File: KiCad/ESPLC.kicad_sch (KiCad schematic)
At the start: 51 parts, among them J1 D1, J10 A2, J11 USB_C_Receptacle_USB2.0_16P, J2 D2, J3 D3, J4 D4, J5 Screw_Terminal_01x03, J6 Screw_Terminal_01x03, J7 Screw_Terminal_01x03, J8 Screw_Terminal_01x03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

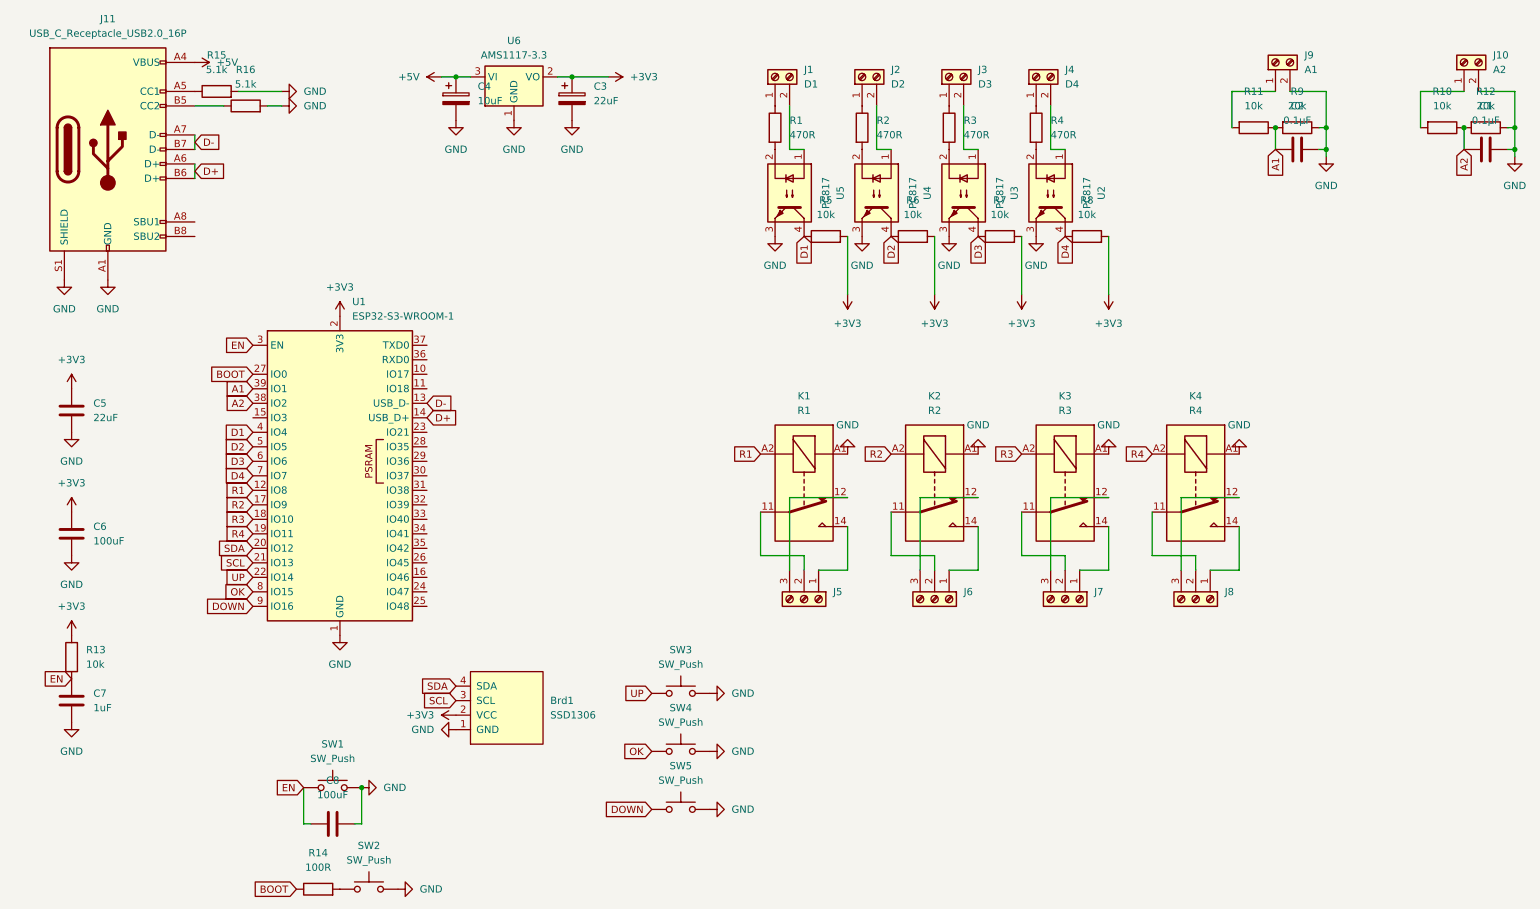
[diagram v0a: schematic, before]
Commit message: Added Software section to README, updated Gerber
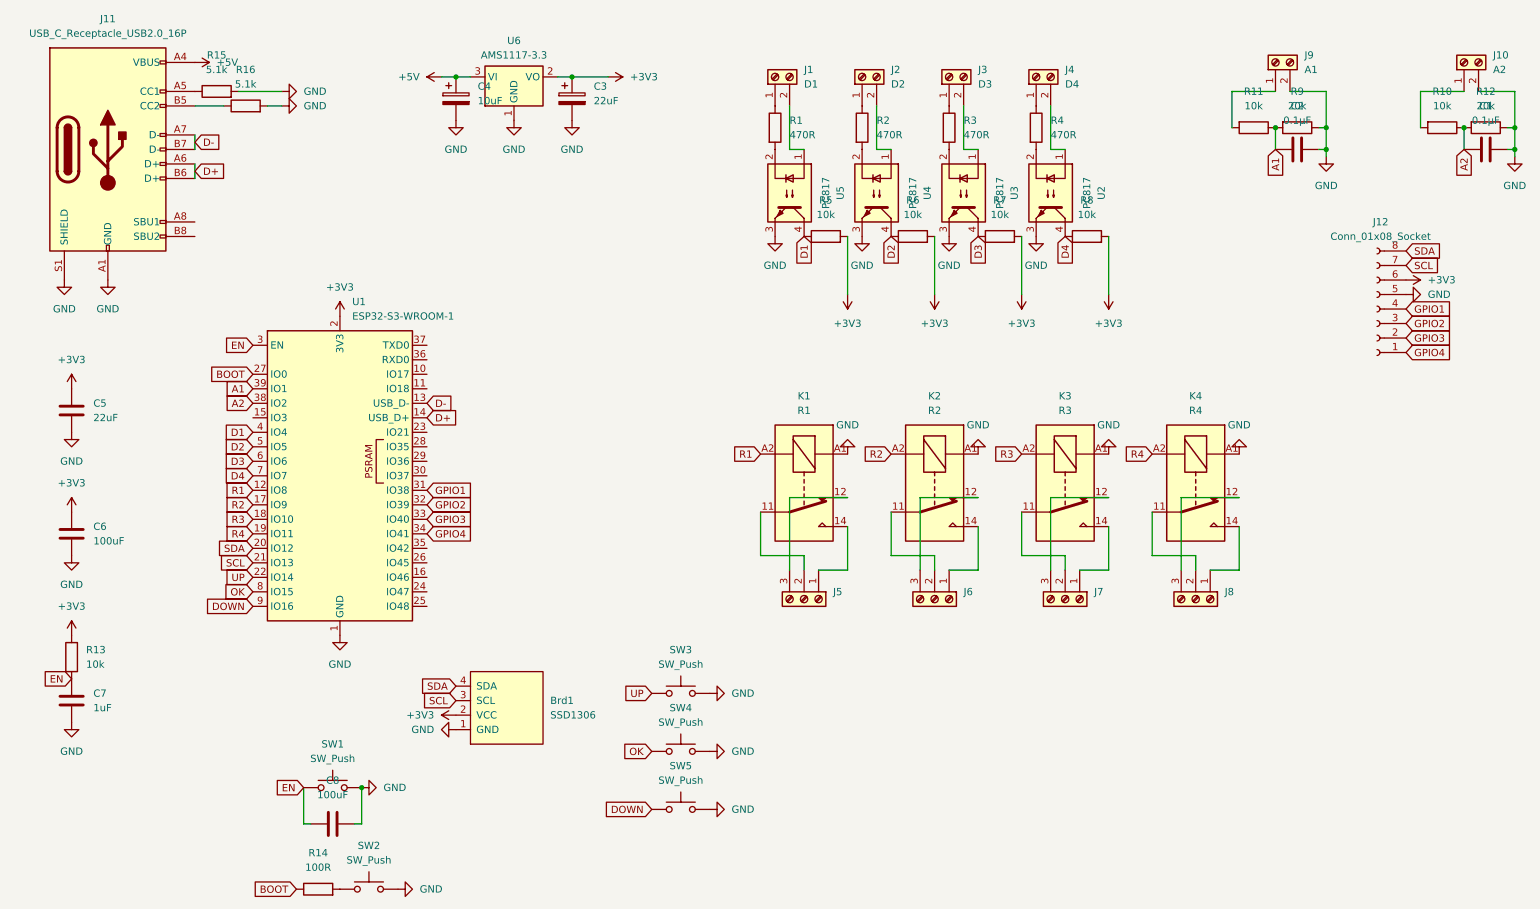
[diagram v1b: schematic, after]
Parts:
- added J12: Conn_01x08_Socket, Connector_PinSocket_2.00mm:PinSocket_1x08_P2.00mm_Horizontal, symbol Connector:Conn_01x08_Socket
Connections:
- net +3V3: now also J12.6 (Pin_6)
- net GND: now also J12.5 (Pin_5)
- net SCL: now also J12.7 (Pin_7)
- net SDA: now also J12.8 (Pin_8)
- net GPIO1: now reaches U1.31 (IO38)
- net GPIO1: now also J12.4 (Pin_4)
- net GPIO2: now reaches U1.32 (IO39)
- net GPIO2: now also J12.3 (Pin_3)
- net GPIO3: now reaches U1.33 (IO40)
- net GPIO3: now also J12.2 (Pin_2)
- net GPIO4: now reaches U1.34 (IO41)
- net GPIO4: now also J12.1 (Pin_1)
